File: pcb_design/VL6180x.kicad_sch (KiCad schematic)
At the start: 6 parts, among them J17 ToF, U4 VL6180XV0NR/1

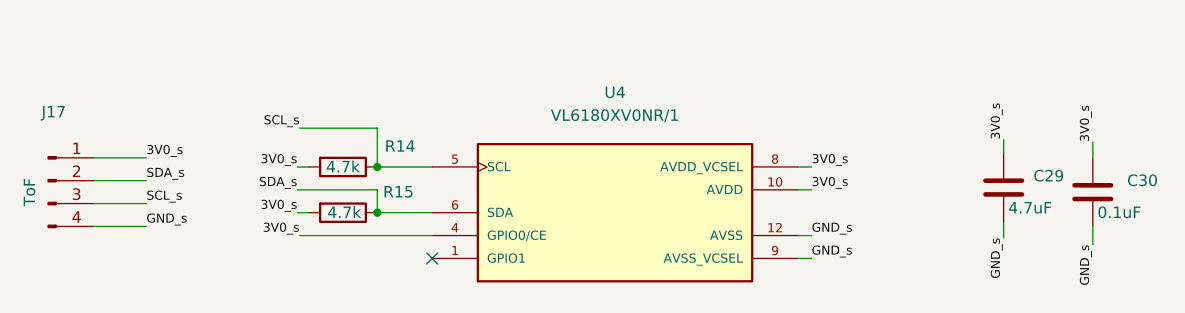
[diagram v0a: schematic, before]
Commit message: Update mushak PCB with new changes * Add AMS1117 as 3.3v regulator * Add new alternate placement for IR sensors * Add new 3.3v compatible ToF sensor * Update gerber files
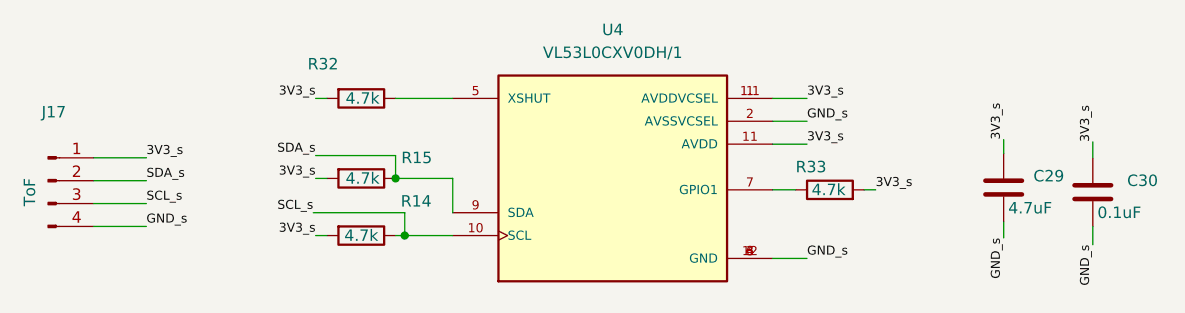
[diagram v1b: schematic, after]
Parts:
- removed U4: VL6180XV0NR/1, VL6180XV0NR_1:LGA12R75P2X6_280X480X110, symbol VL6180XV0NR_1:VL6180XV0NR/1
- added R32, R33: 4.7k, Resistor_SMD:R_0402_1005Metric, symbol Device:R
- added U4: VL53L0CXV0DH/1, VL53L0CXV0DH_1:XDCR_VL53L0CXV0DH_1, symbol VL53L0CXV0DH_1:VL53L0CXV0DH/1
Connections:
- net GND_s: now also U4.12 (GND), U4.2 (AVSSVCSEL), U4.3 (GND), U4.4 (GND), U4.6 (GND)
- net SCL_s: now also U4.10 (SCL)
- net SDA_s: now also U4.9 (SDA)
- net 3V0_s renamed 3V3_s
- net 3V3_s: now also R32.2, R33.2, U4.1 (AVDDVCSEL), U4.1.1 (AVDDVCSEL), U4.11 (AVDD)
- new net: R32.1, U4.5 (XSHUT)
- new net: R33.1, U4.7 (GPIO1)
- no-connect marks 1 -> 0
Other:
- moved on the sheet: R14, R15

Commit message: Add changes to silkscreen and filter capacitors
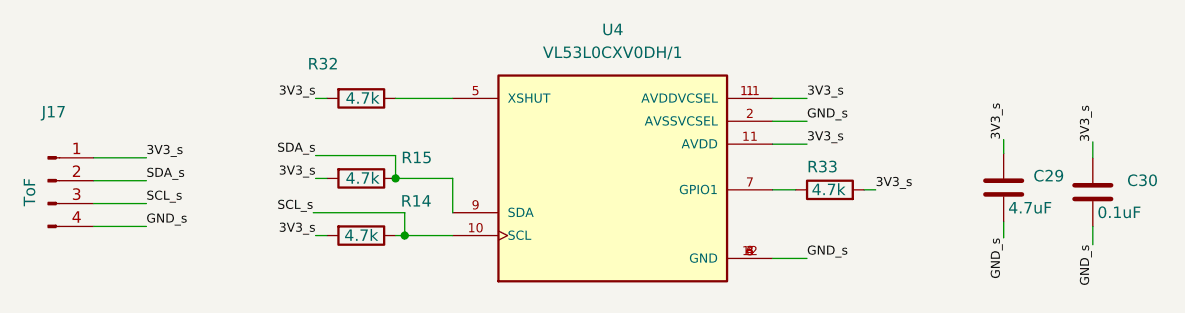
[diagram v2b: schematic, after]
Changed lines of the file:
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@@
   (symbol (lib_id "Device:R") (at 171.45 91.44 90) (unit 1)
     (in_bom yes) (on_board yes)
-    (property "Reference" "R33" (id 0) (at 167.64 88.9 90)
+    (property "Reference" "R33" (id 0) (at 168.91 88.9 90)
       (effects (font (size 1.27 1.27)) (justify right))
     )
